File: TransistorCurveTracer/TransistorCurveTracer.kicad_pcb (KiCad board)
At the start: 2 copper layers, 22 parts, among them J1 Conn_01x04_Pin, Q1 BC547, U1 NE555P, U3 MCP601-xP

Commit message: in progress
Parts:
- added J2: Conn_01x04_Pin, Connector_PinHeader_2.54mm:PinHeader_1x04_P2.54mm_Vertical, F.Cu at (55.5, 15.7)
- added J3: Conn_01x04_Pin, Connector_PinHeader_2.54mm:PinHeader_1x04_P2.54mm_Vertical, F.Cu at (60.2, 15.7)
- moved D2 4.42 mm to (81.5, 32.1)
- moved R5 4.42 mm to (81.5, 26.3)
- moved U3 1.54 mm to (86.4, 29.2)
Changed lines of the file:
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@@
   (net 16 "unconnected-(U3-NC-Pad5)")
   (net 17 "unconnected-(U3-NC-Pad8)")
+  (net 18 "/NC")
   (footprint "Resistor_SMD:R_1206_3216Metric_Pad1.30x1.75mm_HandSolder" (layer "F.Cu")
     (at 71.12 21.818 90)
@@
     )
   )
+  (footprint "Connector_PinHeader_2.54mm:PinHeader_1x04_P2.54mm_Vertical" (layer "F.Cu")
+    (at 55.548 15.748)
+    (descr "Through hole straight pin header, 1x04, 2.54mm pitch, single row")
+    (tags "Through hole pin header THT 1x04 2.54mm single row")
+    (property "Sheetfile" "TransistorCurveTracer.kicad_sch")
+    (property "Sheetname" "")
+    (property "ki_description" "Generic connector, single row, 01x04, script generated")
+    (property "ki_keywords" "connector")
+    (attr through_hole)
+    (fp_text reference "J2" (at 0 -2.33) (layer "F.SilkS")
+        (effects (font (size 1 1) (thickness 0.15)))
+    )
+    (fp_text value "Conn_01x04_Pin" (at 0 9.95) (layer "F.Fab")
+        (effects (font (size 1 1) (thickness 0.15)))
+    )
+    (fp_text user "${REFERENCE}" (at 0 3.81 90) (layer "F.Fab")
+        (effects (font (size 1 1) (thickness 0.15)))
+    )
+    (fp_line (start -1.33 -1.33) (end 0 -1.33)
+      (stroke (width 0.12) (type solid)) (layer "F.SilkS"))
+    (fp_line (start -1.33 0) (end -1.33 -1.33)
+      (stroke (width 0.12) (type solid)) (layer "F.SilkS"))
+    (fp_line (start -1.33 1.27) (end -1.33 8.95)
+      (stroke (width 0.12) (type solid)) (layer "F.SilkS"))
+    (fp_line (start -1.33 1.27) (end 1.33 1.27)
+      (stroke (width 0.12) (type solid)) (layer "F.SilkS"))
+    (fp_line (start -1.33 8.95) (end 1.33 8.95)
+      (stroke (width 0.12) (type solid)) (layer "F.SilkS"))
+    (fp_line (start 1.33 1.27) (end 1.33 8.95)
+      (stroke (width 0.12) (type solid)) (layer "F.SilkS"))
+    (fp_line (start -1.8 -1.8) (end -1.8 9.4)
+      (stroke (width 0.05) (type solid)) (layer "F.CrtYd"))
+    (fp_line (start -1.8 9.4) (end 1.8 9.4)
+      (stroke (width 0.05) (type solid)) (layer "F.CrtYd"))
+    (fp_line (start 1.8 -1.8) (end -1.8 -1.8)
+      (stroke (width 0.05) (type solid)) (layer "F.CrtYd"))
+    (fp_line (start 1.8 9.4) (end 1.8 -1.8)
+      (stroke (width 0.05) (type solid)) (layer "F.CrtYd"))
+    (fp_line (start -1.27 -0.635) (end -0.635 -1.27)
+      (stroke (width 0.1) (type solid)) (layer "F.Fab"))
+    (fp_line (start -1.27 8.89) (end -1.27 -0.635)
+      (stroke (width 0.1) (type solid)) (layer "F.Fab"))
+    (fp_line (start -0.635 -1.27) (end 1.27 -1.27)
+      (stroke (width 0.1) (type solid)) (layer "F.Fab"))
+    (fp_line (start 1.27 -1.27) (end 1.27 8.89)
+      (stroke (width 0.1) (type solid)) (layer "F.Fab"))
+    (fp_line (start 1.27 8.89) (end -1.27 8.89)
+      (stroke (width 0.1) (type solid)) (layer "F.Fab"))
+    (pad "1" thru_hole rect (at 0 0) (size 1.7 1.7) (drill 1) (layers "*.Cu" "*.Mask")
+      (net 9 "/Vcc") (pinfunction "Pin_1") (pintype "passive"))
+    (pad "2" thru_hole oval (at 0 2.54) (size 1.7 1.7) (drill 1) (layers "*.Cu" "*.Mask")
+      (net 2 "GND") (pinfunction "Pin_2") (pintype "passive"))
+    (pad "3" thru_hole oval (at 0 5.08) (size 1.7 1.7) (drill 1) (layers "*.Cu" "*.Mask")
+      (net 7 "/Out555") (pinfunction "Pin_3") (pintype "passive"))
+    (pad "4" thru_hole oval (at 0 7.62) (size 1.7 1.7) (drill 1) (layers "*.Cu" "*.Mask")
+      (net 8 "/Reset555") (pinfunction "Pin_4") (pintype "passive"))
+    (model "${KICAD6_3DMODEL_DIR}/Connector_PinHeader_2.54mm.3dshapes/PinHeader_1x04_P2.54mm_Vertical.wrl"
+      (offset (xyz 0 0 0))
+      (scale (xyz 1 1 1))
+      (rotate (xyz 0 0 0))
+    )
+  )
   (footprint "Resistor_SMD:R_1206_3216Metric_Pad1.30x1.75mm_HandSolder" (layer "F.Cu")
     (at 117.83 35.064)
@@
   )
   (footprint "Diode_SMD:D_1812_4532Metric_Pad1.30x3.40mm_HandSolder" (layer "F.Cu")
-    (at 78.74 28.641 -90)
+    (at 81.534 32.065 -90)
     (descr "Diode SMD 1812 (4532 Metric), square (rectangular) end terminal, IPC_7351 nominal, (Body size source: https://www.nikhef.nl/pub/departments/mt/projects/detectorR_D/dtddice/ERJ2G.pdf), generated with kicad-footprint-generator")
     (tags "diode handsolder")
@@
   )
   (footprint "Resistor_THT:R_Axial_DIN0207_L6.3mm_D2.5mm_P2.54mm_Vertical" (layer "F.Cu")
-    (at 78.74 22.86 90)
+    (at 81.534 26.284 90)
     (descr "Resistor, Axial_DIN0207 series, Axial, Vertical, pin pitch=2.54mm, 0.25W = 1/4W, length*diameter=6.3*2.5mm^2, http://cdn-reichelt.de/documents/datenblatt/B400/1_4W%23YAG.pdf")
     (tags "Resistor Axial_DIN0207 series Axial Vertical pin pitch 2.54mm 0.25W = 1/4W length 6.3mm diameter 2.5mm")
@@
       (net 14 "Net-(R3-Pad2)") (pintype "passive"))
     (model "${KICAD6_3DMODEL_DIR}/Resistor_THT.3dshapes/R_Axial_DIN0207_L6.3mm_D2.5mm_P2.54mm_Vertical.wrl"
+      (offset (xyz 0 0 0))
+      (scale (xyz 1 1 1))
+      (rotate (xyz 0 0 0))
+    )
+  )
+  (footprint "Connector_PinHeader_2.54mm:PinHeader_1x04_P2.54mm_Vertical" (layer "F.Cu")
+    (at 60.198 15.748)
+    (descr "Through hole straight pin header, 1x04, 2.54mm pitch, single row")
+    (tags "Through hole pin header THT 1x04 2.54mm single row")
+    (property "Sheetfile" "TransistorCurveTracer.kicad_sch")
+    (property "Sheetname" "")
+    (property "ki_description" "Generic connector, single row, 01x04, script generated")
+    (property "ki_keywords" "connector")
+    (attr through_hole)
+    (fp_text reference "J3" (at 0 -2.33) (layer "F.SilkS")
+        (effects (font (size 1 1) (thickness 0.15)))
+    )
+    (fp_text value "Conn_01x04_Pin" (at 0 9.95) (layer "F.Fab")
+        (effects (font (size 1 1) (thickness 0.15)))
+    )
+    (fp_text user "${REFERENCE}" (at 0 3.81 90) (layer "F.Fab")
+        (effects (font (size 1 1) (thickness 0.15)))
+    )
+    (fp_line (start -1.33 -1.33) (end 0 -1.33)
+      (stroke (width 0.12) (type solid)) (layer "F.SilkS"))
+    (fp_line (start -1.33 0) (end -1.33 -1.33)
+      (stroke (width 0.12) (type solid)) (layer "F.SilkS"))
+    (fp_line (start -1.33 1.27) (end -1.33 8.95)
+      (stroke (width 0.12) (type solid)) (layer "F.SilkS"))
+    (fp_line (start -1.33 1.27) (end 1.33 1.27)
+      (stroke (width 0.12) (type solid)) (layer "F.SilkS"))
+    (fp_line (start -1.33 8.95) (end 1.33 8.95)
+      (stroke (width 0.12) (type solid)) (layer "F.SilkS"))
+    (fp_line (start 1.33 1.27) (end 1.33 8.95)
+      (stroke (width 0.12) (type solid)) (layer "F.SilkS"))
+    (fp_line (start -1.8 -1.8) (end -1.8 9.4)
+      (stroke (width 0.05) (type solid)) (layer "F.CrtYd"))
+    (fp_line (start -1.8 9.4) (end 1.8 9.4)
+      (stroke (width 0.05) (type solid)) (layer "F.CrtYd"))
+    (fp_line (start 1.8 -1.8) (end -1.8 -1.8)
+      (stroke (width 0.05) (type solid)) (layer "F.CrtYd"))
+    (fp_line (start 1.8 9.4) (end 1.8 -1.8)
+      (stroke (width 0.05) (type solid)) (layer "F.CrtYd"))
+    (fp_line (start -1.27 -0.635) (end -0.635 -1.27)
+      (stroke (width 0.1) (type solid)) (layer "F.Fab"))
+    (fp_line (start -1.27 8.89) (end -1.27 -0.635)
+      (stroke (width 0.1) (type solid)) (layer "F.Fab"))
+    (fp_line (start -0.635 -1.27) (end 1.27 -1.27)
+      (stroke (width 0.1) (type solid)) (layer "F.Fab"))
+    (fp_line (start 1.27 -1.27) (end 1.27 8.89)
+      (stroke (width 0.1) (type solid)) (layer "F.Fab"))
+    (fp_line (start 1.27 8.89) (end -1.27 8.89)
+      (stroke (width 0.1) (type solid)) (layer "F.Fab"))
+    (pad "1" thru_hole rect (at 0 0) (size 1.7 1.7) (drill 1) (layers "*.Cu" "*.Mask")
+      (net 9 "/Vcc") (pinfunction "Pin_1") (pintype "passive"))
+    (pad "2" thru_hole oval (at 0 2.54) (size 1.7 1.7) (drill 1) (layers "*.Cu" "*.Mask")
+      (net 2 "GND") (pinfunction "Pin_2") (pintype "passive"))
+    (pad "3" thru_hole oval (at 0 5.08) (size 1.7 1.7) (drill 1) (layers "*.Cu" "*.Mask")
+      (net 18 "/NC") (pinfunction "Pin_3") (pintype "passive"))
+    (pad "4" thru_hole oval (at 0 7.62) (size 1.7 1.7) (drill 1) (layers "*.Cu" "*.Mask")
+      (net 8 "/Reset555") (pinfunction "Pin_4") (pintype "passive"))
+    (model "${KICAD6_3DMODEL_DIR}/Connector_PinHeader_2.54mm.3dshapes/PinHeader_1x04_P2.54mm_Vertical.wrl"
       (offset (xyz 0 0 0))
       (scale (xyz 1 1 1))
@@
   )
   (footprint "Package_DIP:DIP-8_W7.62mm" (layer "F.Cu")
-    (at 84.846 29.474)
+    (at 86.36 29.21)
     (descr "8-lead though-hole mounted DIP package, row spacing 7.62 mm (300 mils)")
     (tags "THT DIP DIL PDIP 2.54mm 7.62mm 300mil")

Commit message: in progress
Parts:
- added Q2: BC547, Package_TO_SOT_THT:TO-92_Inline, F.Cu at (121.4, 41.7)
- moved J3 48.3 mm to (108.2, 20.8), turned to 90 degrees
- moved Q1 35.9 mm to (121.2, 28.7)
- moved R2 28.8 mm to (104.9, 45.9), turned to -90 degrees
- moved R4 24.5 mm to (92.5, 33.9)
- moved D1 24.5 mm to (92.5, 40.6)
- moved U3 23.6 mm to (110.0, 29.7)
- moved R5 19.9 mm to (99.3, 35.1)
- moved J2 19.7 mm to (35.8, 16.3), turned to 90 degrees
- moved D2 19.7 mm to (99.3, 40.6)
- moved R10 17.2 mm to (122.7, 21.8), turned to 90 degrees
- moved R3 15.8 mm to (109.7, 43.9)
- moved R1 10.1 mm to (104.9, 29.4), turned to 90 degrees
- moved C1 9.53 mm to (92.7, 47.0), turned to -90 degrees
- moved R7 9.41 mm to (117.6, 44.5), turned to -90 degrees
- moved R6 5.70 mm to (122.7, 34.8)
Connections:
- J3 pad 3: /NC -> /ResetStairStep
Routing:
- net GND: track 0.00 -> 108.9 mm, vias 0 -> 1
- net Net-(R3-Pad2): track 0.00 -> 62.8 mm, vias 0 -> 2
- net /ResetStairStep: track 0.00 -> 62.0 mm, vias 0 -> 2
- net /Vcc: track 0.00 -> 48.9 mm
- net Net-(D1-K): track 0.00 -> 24.5 mm, vias 0 -> 1
- net Net-(U3--): track 0.00 -> 24.0 mm
- net /Pulse1: track 0.00 -> 21.4 mm
- net /Reset555: track 0.00 -> 16.0 mm
- net Net-(D2-K): track 0.00 -> 3.30 mm
- net Net-(D1-A): track 0.00 -> 2.93 mm

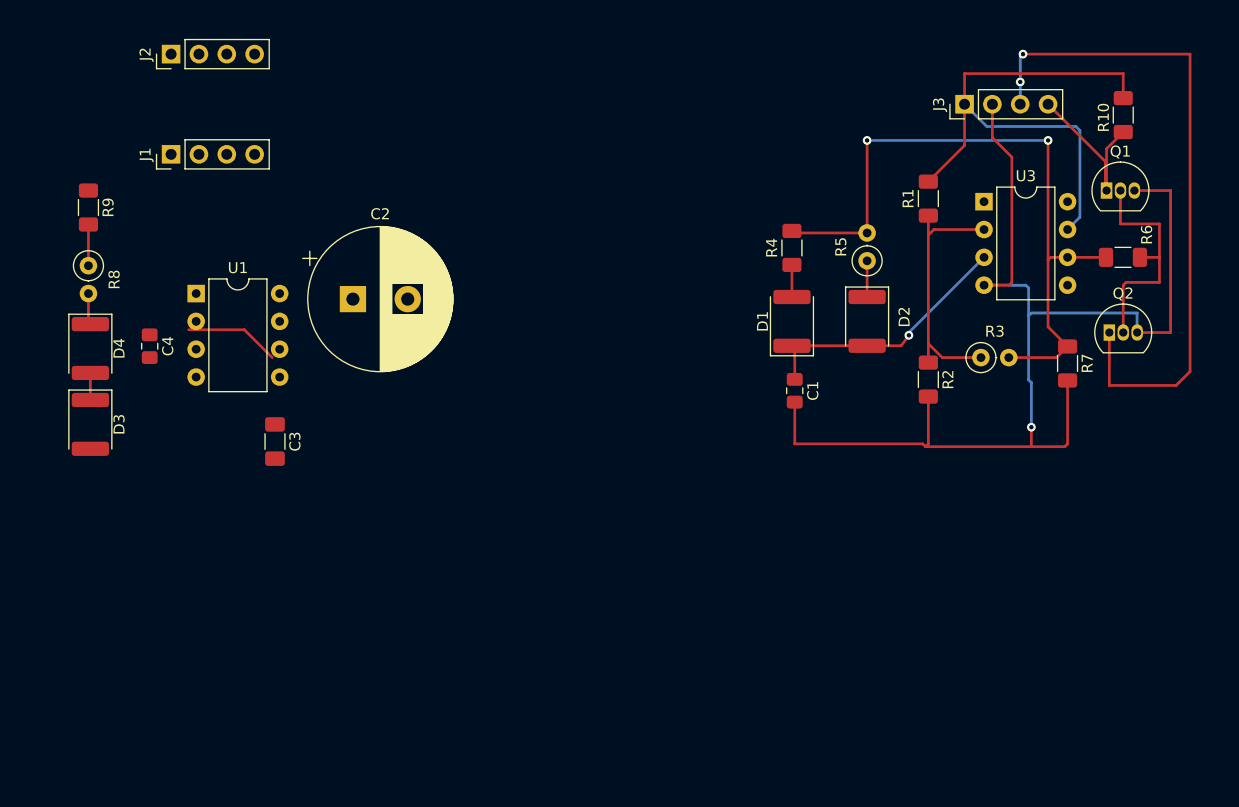
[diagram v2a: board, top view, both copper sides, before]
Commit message: fix VCC/GND VDD/VSS in progress
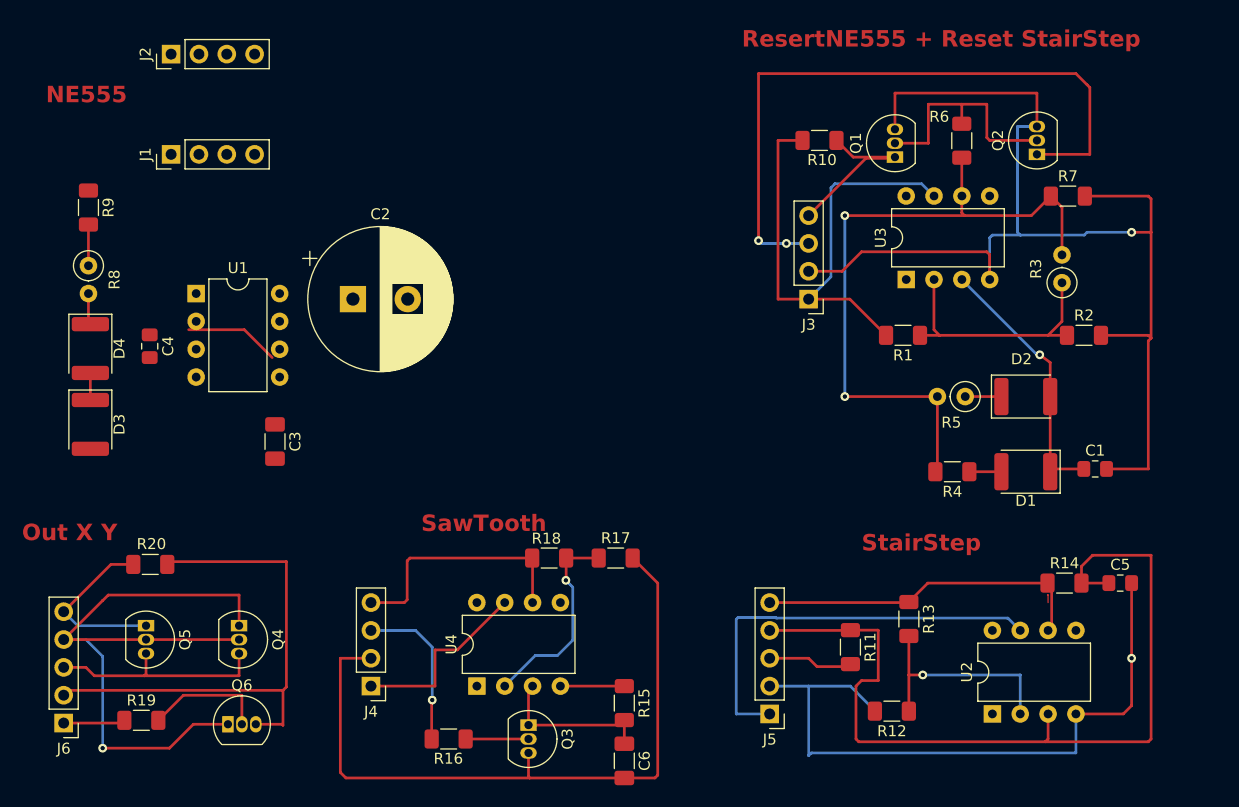
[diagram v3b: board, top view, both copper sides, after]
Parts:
- added C5: 100n, Capacitor_SMD:C_0805_2012Metric_Pad1.18x1.45mm_HandSolder, F.Cu at (122.4, 64.5)
- added C6: 10n, Capacitor_SMD:C_1206_3216Metric_Pad1.33x1.80mm_HandSolder, F.Cu at (77.2, 80.7)
- added J4: Conn_01x04_Pin, Connector_PinHeader_2.54mm:PinHeader_1x04_P2.54mm_Vertical, F.Cu at (54.0, 73.9)
- added J5: Conn_01x05_Pin, Connector_PinHeader_2.54mm:PinHeader_1x05_P2.54mm_Vertical, F.Cu at (90.4, 76.5)
- added J6: Conn_01x05_Pin, Connector_PinHeader_2.54mm:PinHeader_1x05_P2.54mm_Vertical, F.Cu at (26.0, 77.3)
- added Q3: BC547, Package_TO_SOT_THT:TO-92_Inline, F.Cu at (68.4, 77.5)
- added Q4: 2N2907, Package_TO_SOT_THT:TO-92_Inline, F.Cu at (42.0, 68.4)
- added Q5: 2N2907, Package_TO_SOT_THT:TO-92_Inline, F.Cu at (33.5, 68.4)
- added Q6: DUT, Package_TO_SOT_THT:TO-92_Inline, F.Cu at (41.0, 77.4)
- added R11: 10k, Resistor_SMD:R_1206_3216Metric_Pad1.30x1.75mm_HandSolder, F.Cu at (97.8, 70.4)
- added R12: 10k, Resistor_SMD:R_1206_3216Metric_Pad1.30x1.75mm_HandSolder, F.Cu at (101.6, 76.2)
- added R13: 10k, Resistor_SMD:R_1206_3216Metric_Pad1.30x1.75mm_HandSolder, F.Cu at (103.1, 67.8)
- added R14: 10k, Resistor_SMD:R_1206_3216Metric_Pad1.30x1.75mm_HandSolder, F.Cu at (117.3, 64.5)
- added R15: 10k, Resistor_SMD:R_1206_3216Metric_Pad1.30x1.75mm_HandSolder, F.Cu at (77.2, 75.5)
- added R16: 3.9k, Resistor_SMD:R_1206_3216Metric_Pad1.30x1.75mm_HandSolder, F.Cu at (61.1, 78.7)
- added R17: 3.9k, Resistor_SMD:R_1206_3216Metric_Pad1.30x1.75mm_HandSolder, F.Cu at (76.4, 62.2)
- added R18: 10k, Resistor_SMD:R_1206_3216Metric_Pad1.30x1.75mm_HandSolder, F.Cu at (70.3, 62.2)
- added R19: 470k, Resistor_SMD:R_1206_3216Metric_Pad1.30x1.75mm_HandSolder, F.Cu at (33.1, 77.0)
- added R20: 270k, Resistor_SMD:R_1206_3216Metric_Pad1.30x1.75mm_HandSolder, F.Cu at (33.9, 62.8)
- added U2: MCP601-xP, Package_DIP:DIP-8_W7.62mm, F.Cu at (110.7, 76.5)
- added U4: MCP601-xP, Package_DIP:DIP-8_W7.62mm, F.Cu at (63.7, 73.9)
- moved C1 28.3 mm to (120.1, 54.1), turned to 0 degrees
- moved R10 27.8 mm to (95.0, 24.1), turned to 180 degrees
- moved D1 25.4 mm to (113.8, 54.4), turned to 180 degrees
- moved R4 25.1 mm to (107.1, 54.4), turned to 180 degrees
- moved J3 22.8 mm to (94.0, 38.6), turned to 180 degrees
- moved Q1 19.5 mm to (101.9, 25.7), turned to 90 degrees
- moved R6 18.2 mm to (108.0, 24.2), turned to 90 degrees
- moved Q2 17.5 mm to (114.8, 25.4), turned to 90 degrees
- moved D2 16.0 mm to (113.8, 47.5), turned to 0 degrees
- moved R5 15.3 mm to (108.3, 47.5), turned to 180 degrees
- moved R7 15.3 mm to (117.6, 29.2), turned to 0 degrees
- moved R2 14.8 mm to (119.1, 41.9), turned to 0 degrees
- moved R1 12.7 mm to (102.6, 41.9), turned to 180 degrees
- moved R3 10.1 mm to (117.1, 37.1), turned to 90 degrees
- moved U3 10.0 mm to (102.9, 36.8), turned to 90 degrees
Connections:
- R1 pad 1: Net-(U3--) -> Net-(U3-+)
- R2 pad 1: Net-(U3--) -> Net-(U3-+)
- R3 pad 1: Net-(U3--) -> Net-(U3-+)
- U3 pad 2: Net-(U3--) -> Net-(D1-K)
- U3 pad 3: Net-(D1-K) -> Net-(U3-+)
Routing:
- net GND: track 108.9 -> 284.7 mm, vias 1 -> 2
- net /ResetStairStep: track 62.0 -> 140.9 mm
- net /X: track 0.00 -> 61.4 mm, vias 0 -> 1
- net /Vcc: track 48.9 -> 110.2 mm
- net /SawTooth: track 0.00 -> 43.0 mm
- net /StairStep: track 0.00 -> 36.3 mm
- net (no net): track 0.00 -> 24.8 mm
- net Net-(U3--): track 24.0 -> 0.00 mm
- net /Out555: track 0.00 -> 22.4 mm, vias 0 -> 1
- net Net-(U2--): track 0.00 -> 20.6 mm, vias 0 -> 1
- net Net-(U4--): track 0.00 -> 18.7 mm, vias 0 -> 1
- net /Y: track 0.00 -> 16.2 mm
- net Net-(Q3-C): track 0.00 -> 14.8 mm
- net Net-(Q6-B): track 0.00 -> 11.2 mm
- net Net-(Q3-B): track 0.00 -> 5.74 mm
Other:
- board text added: "NE555"
- board text added: "Out X Y"
- board text added: "ResertNE555 + Reset StairStep"
- board text added: "SawTooth"
- board text added: "StairStep"

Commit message: fixes
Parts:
- C5, R11, R14, R15, R16, R17, R18: moved to B.Cu
- moved R14 17.5 mm to (111.0, 80.8)
- moved C5 17.3 mm to (116.6, 80.8)
- moved R15 10.8 mm to (67.8, 70.1), turned to 0 degrees
- moved R16 8.84 mm to (58.4, 70.3), turned to 90 degrees
- moved Q3 7.72 mm to (60.7, 77.5)
- moved C6 7.71 mm to (70.1, 77.7), turned to 0 degrees
- moved R13 4.12 mm to (106.8, 69.7)
- moved R11 2.50 mm to (95.3, 70.2)
- moved R12 1.50 mm to (100.1, 76.2), turned to -90 degrees
- moved R17 1.26 mm to (76.2, 63.5), turned to -90 degrees
- moved U2 1.08 mm to (110.0, 77.2)
- moved R18 0.26 mm to (70.3, 62.0)
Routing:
- net GND: track 284.7 -> 253.9 mm, vias 2 -> 1
- net /ResetStairStep: track 140.9 -> 110.3 mm
- net /Vcc: track 110.2 -> 94.5 mm
- net /StairStep: track 36.3 -> 49.3 mm
- net /Out555: track 22.4 -> 10.3 mm, vias 1 -> 0
- net Net-(U4--): track 18.7 -> 28.6 mm, vias 1 -> 0
- net Net-(U2--): track 20.6 -> 16.5 mm, vias 1 -> 0
- net Net-(Q3-B): track 5.74 -> 9.14 mm
- net Net-(Q3-C): track 14.8 -> 17.0 mm
- net /SawTooth: track 43.0 -> 41.3 mm
- net (no net): track 24.8 -> 24.1 mm
